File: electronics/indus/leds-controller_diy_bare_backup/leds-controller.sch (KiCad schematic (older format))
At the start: 19 parts, among them P1 ALIM_12V_60V, P10 THERM_LEDS, P2 MICRO_CTRL, P3 FANS, P4 POT_COLOR2, P5 POT_COLOR3, P6 POT_COLOR4, P7 POT_COLOR1, P8 LED+, P9 LED-

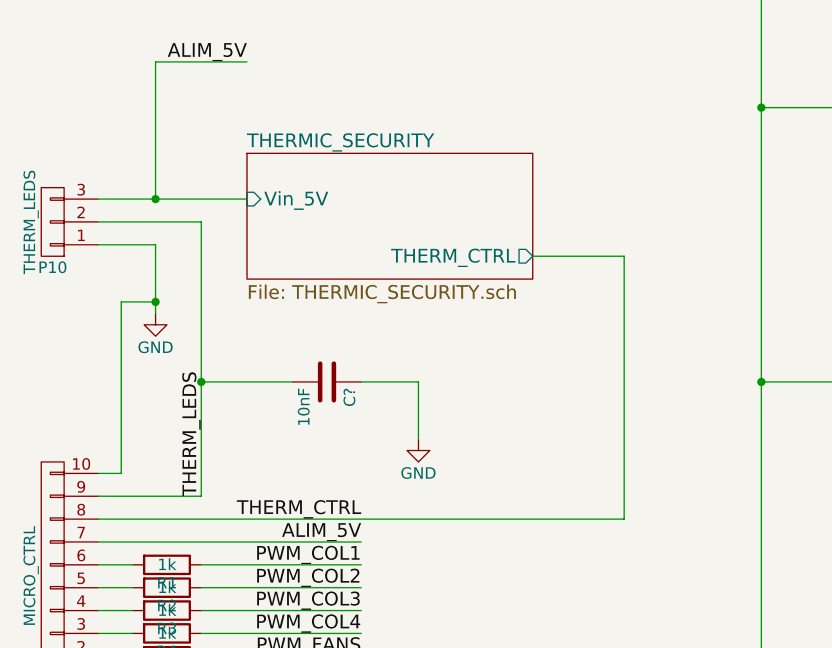
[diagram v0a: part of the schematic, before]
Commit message: simpler schematics with a lot of values now
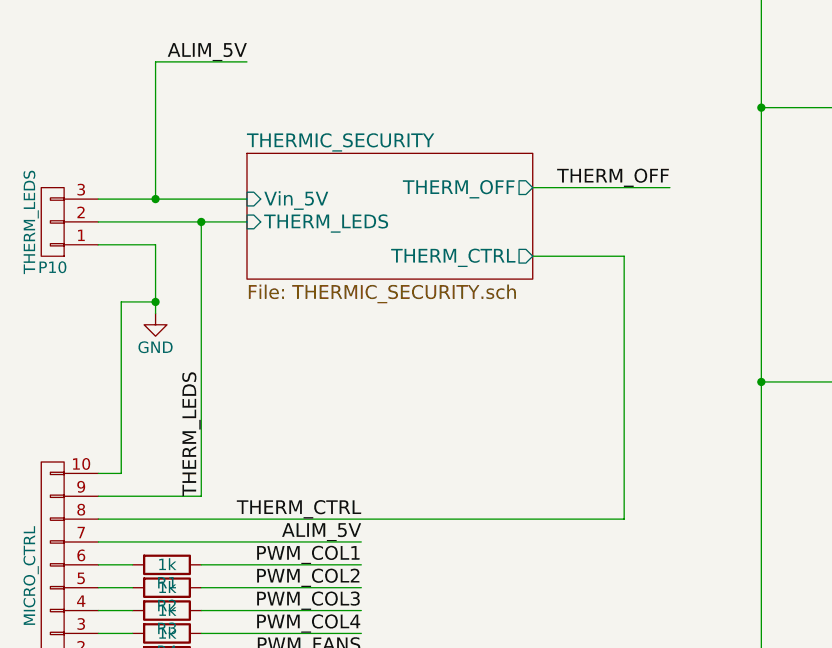
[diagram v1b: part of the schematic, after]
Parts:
- removed C?: 10nF, symbol C
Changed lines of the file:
@@
 F1 "THERMIC_SECURITY.sch" 60
 F2 "Vin_5V" I L 1700 3650 60
-F3 "THERM_CTRL" O R 2950 3900 60
+F3 "THERM_OFF" O R 2950 3600 60
+F4 "THERM_LEDS" I L 1700 3750 60
+F5 "THERM_CTRL" O R 2950 3900 60
 $EndSheet
 $Comp
@@
 $EndComp
 Text Label 4350 2200 0    60   ~ 0
+THERM_OFF
+Text Label 3550 3600 2    60   ~ 0
 THERM_OFF
 Text Label 2200 5250 2    60   ~ 0
@@
 	5150 1900 4350 1900
 Wire Wire Line
+	2950 3600 3550 3600
+Wire Wire Line
 	1050 3650 1700 3650
+Wire Wire Line
+	1050 3750 1700 3750
 Wire Wire Line
 	5150 2050 3950 2050
@@
 Wire Wire Line
 	1500 4950 1050 4950
+Connection ~ 1500 3750
 Text Label 4350 4750 0    60   ~ 0
 REG_1.2A
@@
 Text Notes 800  2750 0    60   ~ 0
 SECURITE THERMIQUE\n- les controlleurs s'arrètent à une certaine T°\n- la T° des cartes de leds est prise en compte aussi
-Wire Wire Line
-	1500 4450 1900 4450
-Connection ~ 1500 4450
-$Comp
-L C C?
-U 1 1 57683C7B
-P 2050 4450
-F 0 "C?" H 2075 4550 50  0000 L CNN
-F 1 "10nF" H 2075 4350 50  0000 L CNN
-F 2 "" H 2088 4300 50  0000 C CNN
-F 3 "" H 2050 4450 50  0000 C CNN
-	1    2050 4450
-	0    1    1    0
-$EndComp
-$Comp
-L GND #PWR?
-U 1 1 576840C0
-P 2450 4700
-F 0 "#PWR?" H 2450 4450 50  0001 C CNN
-F 1 "GND" H 2450 4550 50  0000 C CNN
-F 2 "" H 2450 4700 50  0000 C CNN
-F 3 "" H 2450 4700 50  0000 C CNN
-	1    2450 4700
-	1    0    0    -1
-$EndComp
-Wire Wire Line
-	2200 4450 2450 4450
-Wire Wire Line
-	2450 4450 2450 4700
-Wire Wire Line
-	1050 3750 1500 3750
 $EndSCHEMATC
